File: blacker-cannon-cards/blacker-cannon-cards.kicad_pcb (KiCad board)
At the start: 2 copper layers, 85 x 55 mm, 2 parts

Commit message: Add soldermask footprint for beta
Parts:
- added G***: LOGO, npfa-gdbg:F_beta_mask_403dpi, F.Cu at (92.5, 77.5)
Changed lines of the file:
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@@
     (tracks 0)
     (zones 0)
-    (modules 2)
+    (modules 3)
     (nets 1)
   )
@@
     (uvia_drill 0.1)
   )
+  (module npfa-gdbg:F_beta_mask_403dpi (layer F.Cu)
+    (at 92.5 77.5)
+    (fp_text reference G*** (at 0 0) (layer F.SilkS) hide
+      (effects (font (size 1.524 1.524) (thickness 0.3)))
+    )
+    (fp_text value LOGO (at 0.75 0) (layer F.SilkS) hide
+      (effects (font (size 1.524 1.524) (thickness 0.3)))
+    )
+    (fp_poly (pts (xy 32.227408 -4.819358) (xy 32.535706 -4.69041) (xy 32.784801 -4.451038) (xy 32.827088 -4.390906)
+      (xy 32.899712 -4.272928) (xy 32.947698 -4.161016) (xy 32.976113 -4.025469) (xy 32.990026 -3.83659)
+      (xy 32.994502 -3.564677) (xy 32.994789 -3.408077) (xy 32.991513 -3.074074) (xy 32.978466 -2.832117)
+      (xy 32.950821 -2.648296) (xy 32.90375 -2.488699) (xy 32.843158 -2.342984) (xy 32.749223 -2.152467)
+      (xy 32.675218 -2.0578) (xy 32.599291 -2.035903) (xy 32.559535 -2.043405) (xy 32.420993 -2.071941)
+      (xy 32.216129 -2.104159) (xy 32.098499 -2.119676) (xy 31.837109 -2.120552) (xy 31.631524 -2.064004)
+      (xy 31.496214 -1.965455) (xy 31.445648 -1.840329) (xy 31.494295 -1.704052) (xy 31.610749 -1.599722)
+      (xy 31.732101 -1.542244) (xy 31.889873 -1.518741) (xy 32.122254 -1.52485) (xy 32.208043 -1.531452)
+      (xy 32.645209 -1.568103) (xy 32.833902 -1.339186) (xy 33.055745 -0.993254) (xy 33.234848 -0.563141)
+      (xy 33.362199 -0.086127) (xy 33.428786 0.400511) (xy 33.425598 0.859494) (xy 33.404099 1.019568)
+      (xy 33.344162 1.283237) (xy 33.264307 1.541713) (xy 33.207124 1.68321) (xy 32.981107 2.02351)
+      (xy 32.682619 2.269057) (xy 32.330279 2.412232) (xy 31.942707 2.445414) (xy 31.545161 2.36335)
+      (xy 31.35259 2.262869) (xy 31.146453 2.107654) (xy 31.053742 2.018737) (xy 30.814433 1.763306)
+      (xy 30.833147 -1.119464) (xy 30.83786 -1.801376) (xy 30.842697 -2.368898) (xy 30.848172 -2.833693)
+      (xy 30.854801 -3.207424) (xy 30.863098 -3.501756) (xy 30.873579 -3.728353) (xy 30.886758 -3.898877)
+      (xy 30.903151 -4.024992) (xy 30.923272 -4.118362) (xy 30.947637 -4.19065) (xy 30.971028 -4.242143)
+      (xy 31.184483 -4.54193) (xy 31.473638 -4.742293) (xy 31.829453 -4.83713) (xy 31.856148 -4.83962)
+      (xy 32.227408 -4.819358)) (layer F.Mask) (width 0.01))
+    (fp_poly (pts (xy 40.746813 0) (xy 36.272208 4.474938) (xy 35.6484 5.098482) (xy 35.049783 5.69624)
+      (xy 34.482362 6.262251) (xy 33.952141 6.790551) (xy 33.465122 7.27518) (xy 33.027311 7.710176)
+      (xy 32.64471 8.089576) (xy 32.323324 8.407419) (xy 32.069157 8.657743) (xy 31.888213 8.834585)
+      (xy 31.786495 8.931985) (xy 31.765756 8.949876) (xy 31.717706 8.906267) (xy 31.58661 8.779423)
+      (xy 31.378483 8.575315) (xy 31.09934 8.299916) (xy 30.755195 7.959198) (xy 30.352063 7.559134)
+      (xy 29.895959 7.105696) (xy 29.392896 6.604856) (xy 28.84889 6.062586) (xy 28.269955 5.48486)
+      (xy 27.88172 5.097033) (xy 29.642731 5.097033) (xy 29.66886 5.139189) (xy 29.755053 5.160222)
+      (xy 29.925413 5.167458) (xy 30.119111 5.168238) (xy 30.617796 5.168238) (xy 30.69066 4.774318)
+      (xy 30.718994 4.569504) (xy 30.747625 4.272722) (xy 30.773837 3.918024) (xy 30.794912 3.539461)
+      (xy 30.801397 3.386312) (xy 30.83927 2.392227) (xy 30.97162 2.490259) (xy 31.362689 2.704946)
+      (xy 31.813252 2.825269) (xy 32.296132 2.848393) (xy 32.78415 2.771483) (xy 33.002093 2.702028)
+      (xy 33.381878 2.502552) (xy 33.741414 2.208051) (xy 34.048127 1.848953) (xy 34.219087 1.565245)
+      (xy 34.427678 1.027591) (xy 34.522226 0.491316) (xy 34.505964 -0.029643) (xy 34.382125 -0.521345)
+      (xy 34.153945 -0.969852) (xy 33.824657 -1.361225) (xy 33.477194 -1.632485) (xy 33.175241 -1.826248)
+      (xy 33.500605 -2.162168) (xy 33.775751 -2.504121) (xy 33.946129 -2.866736) (xy 34.024589 -3.282887)
+      (xy 34.033355 -3.524999) (xy 33.975794 -3.989551) (xy 33.81183 -4.394554) (xy 33.549609 -4.733072)
+      (xy 33.197276 -4.998174) (xy 32.762975 -5.182925) (xy 32.254853 -5.280393) (xy 31.954838 -5.294293)
+      (xy 31.43413 -5.247205) (xy 30.980339 -5.101818) (xy 30.574328 -4.851945) (xy 30.56584 -4.845267)
+      (xy 30.27622 -4.555881) (xy 30.066757 -4.201489) (xy 29.928278 -3.763656) (xy 29.876248 -3.459449)
+      (xy 29.864843 -3.308956) (xy 29.854053 -3.045755) (xy 29.844088 -2.683193) (xy 29.835159 -2.234615)
+      (xy 29.827474 -1.713367) (xy 29.821245 -1.132796) (xy 29.816681 -0.506247) (xy 29.813992 0.152933)
+      (xy 29.81338 0.535732) (xy 29.812047 1.360555) (xy 29.809002 2.070257) (xy 29.803853 2.675765)
+      (xy 29.796211 3.188005) (xy 29.785683 3.617905) (xy 29.771878 3.976391) (xy 29.754405 4.274389)
+      (xy 29.732872 4.522827) (xy 29.706889 4.732632) (xy 29.676064 4.914729) (xy 29.652563 5.026427)
+      (xy 29.642731 5.097033) (xy 27.88172 5.097033) (xy 27.662105 4.877649) (xy 27.274895 4.490529)
+      (xy 22.81588 0.031183) (xy 27.306741 -4.459348) (xy 31.797601 -8.949878) (xy 40.746813 0)) (layer F.Mask) (width 0.01))
+  )
   (module npfa-gdbg:F_silk_403dpi (layer F.Cu)

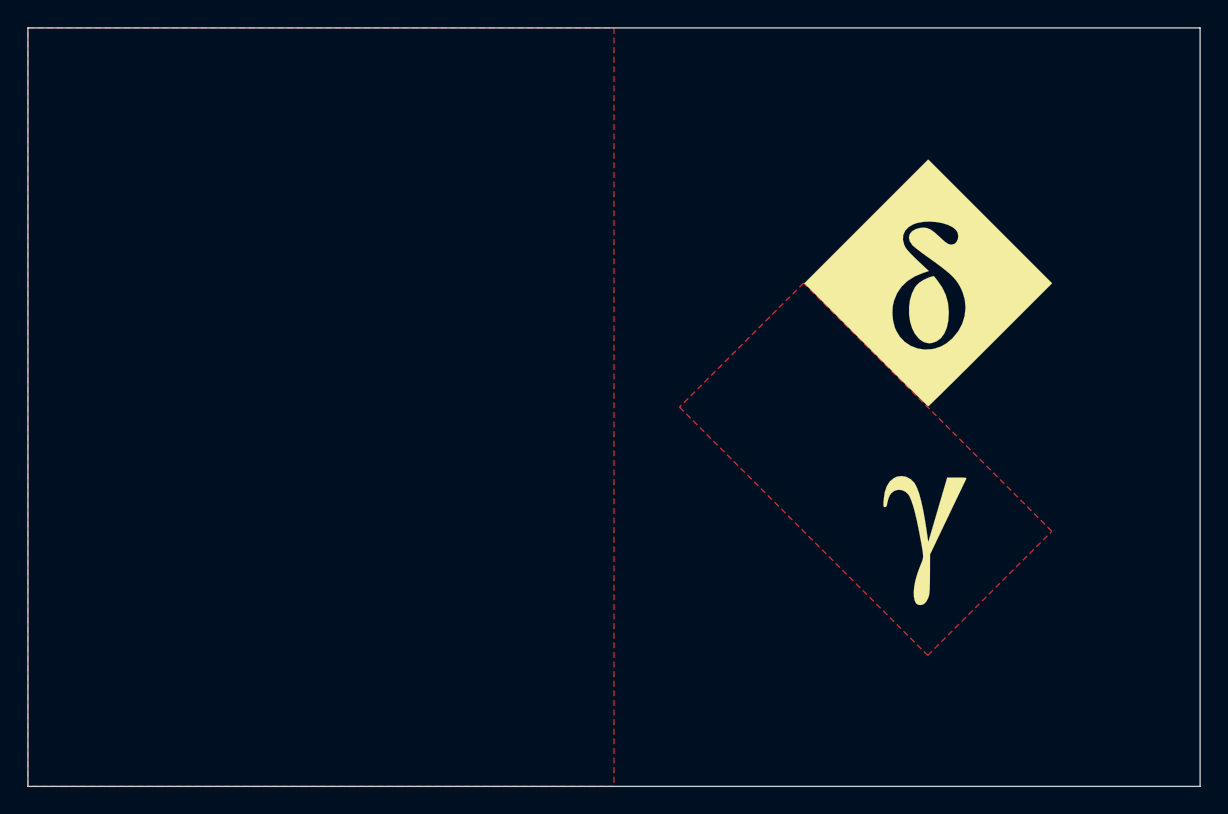
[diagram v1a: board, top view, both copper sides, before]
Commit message: Center diamond on right side
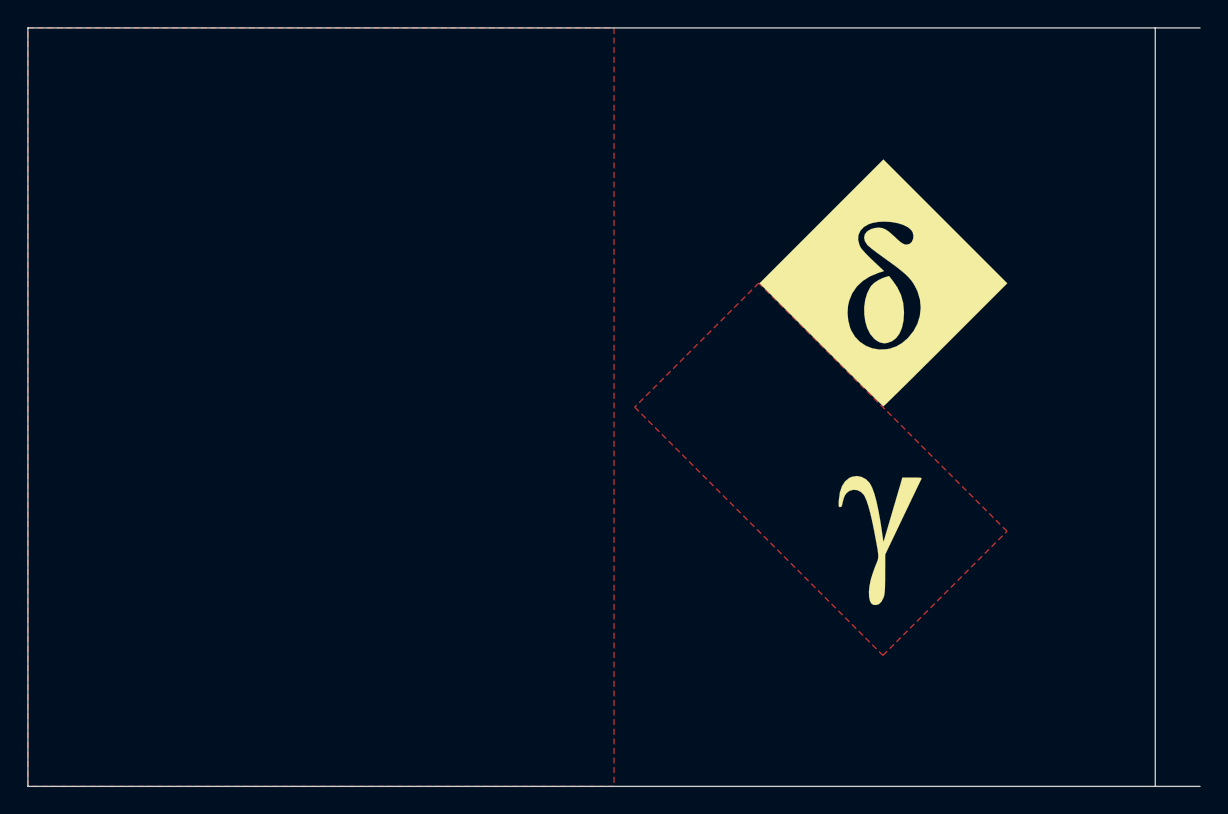
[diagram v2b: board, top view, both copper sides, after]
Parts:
- moved G*** 3.25 mm to (89.2, 77.5) (x3)
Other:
- outline, holes or cut-outs redrawn
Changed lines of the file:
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@@
     (solder_mask_min_width 0.25)
     (aux_axis_origin 0 0)
-    (visible_elements FFFFFF7F)
+    (visible_elements 7FFFFFFF)
     (pcbplotparams
       (layerselection 0x010fc_ffffffff)
@@
   )
   (module npfa-gdbg:F_beta_mask_403dpi (layer F.Cu)
-    (at 92.5 77.5)
+    (at 89.25 77.5)
     (fp_text reference G*** (at 0 0) (layer F.SilkS) hide
       (effects (font (size 1.524 1.524) (thickness 0.3)))
@@
   )
   (module npfa-gdbg:F_silk_403dpi (layer F.Cu)
-    (at 92.5 77.5)
+    (at 89.25 77.5)
     (fp_text reference G*** (at 0 0) (layer F.SilkS) hide
       (effects (font (size 1.524 1.524) (thickness 0.3)))
@@
   )
   (module npfa-gdbg:F_gamma_eng_fp_403dpi (layer F.Cu)
-    (at 92.5 77.5)
+    (at 89.25 77.5)
     (fp_text reference G*** (at 0 0) (layer F.SilkS) hide
       (effects (font (size 1.524 1.524) (thickness 0.3)))
@@
   )
   (gr_line (start 135 50) (end 50 50) (layer Edge.Cuts) (width 0.05))
-  (gr_line (start 135 105) (end 135 50) (layer Edge.Cuts) (width 0.05))
+  (gr_line (start 131.75 105) (end 131.75 50) (layer Edge.Cuts) (width 0.05))
   (gr_line (start 50 105) (end 135 105) (layer Edge.Cuts) (width 0.05))
   (gr_line (start 50 50) (end 50 105) (layer Edge.Cuts) (width 0.05))
@@
   )
   (gr_line (start 135 50) (end 50 50) (layer Dwgs.User) (width 0.15))
-  (gr_line (start 135 105) (end 135 50) (layer Dwgs.User) (width 0.15))
+  (gr_line (start 131.75 105) (end 131.75 50) (layer Dwgs.User) (width 0.15))
   (gr_line (start 50 105) (end 135 105) (layer Dwgs.User) (width 0.15))
   (gr_line (start 50 50) (end 50 105) (layer Dwgs.User) (width 0.15))
@@
     (polygon
       (pts
-        (xy 97.25 77.5) (xy 115.25 95.5) (xy 124.25 86.5) (xy 106.25 68.5)
+        (xy 94 77.5) (xy 112 95.5) (xy 121 86.5) (xy 103 68.5)
       )
     )

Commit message: Actually center it
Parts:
- moved G*** 2.00 mm to (91.2, 77.5) (x3)
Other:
- outline, holes or cut-outs redrawn
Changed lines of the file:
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@@
   )
   (module npfa-gdbg:F_beta_mask_403dpi (layer F.Cu)
-    (at 89.25 77.5)
+    (at 91.25 77.5)
     (fp_text reference G*** (at 0 0) (layer F.SilkS) hide
       (effects (font (size 1.524 1.524) (thickness 0.3)))
@@
   )
   (module npfa-gdbg:F_silk_403dpi (layer F.Cu)
-    (at 89.25 77.5)
+    (at 91.25 77.5)
     (fp_text reference G*** (at 0 0) (layer F.SilkS) hide
       (effects (font (size 1.524 1.524) (thickness 0.3)))
@@
   )
   (module npfa-gdbg:F_gamma_eng_fp_403dpi (layer F.Cu)
-    (at 89.25 77.5)
+    (at 91.25 77.5)
     (fp_text reference G*** (at 0 0) (layer F.SilkS) hide
       (effects (font (size 1.524 1.524) (thickness 0.3)))
@@
   )
   (gr_line (start 135 50) (end 50 50) (layer Edge.Cuts) (width 0.05))
-  (gr_line (start 131.75 105) (end 131.75 50) (layer Edge.Cuts) (width 0.05))
+  (gr_line (start 135 105) (end 135 50) (layer Edge.Cuts) (width 0.05))
   (gr_line (start 50 105) (end 135 105) (layer Edge.Cuts) (width 0.05))
   (gr_line (start 50 50) (end 50 105) (layer Edge.Cuts) (width 0.05))
@@
   )
   (gr_line (start 135 50) (end 50 50) (layer Dwgs.User) (width 0.15))
-  (gr_line (start 131.75 105) (end 131.75 50) (layer Dwgs.User) (width 0.15))
+  (gr_line (start 135 105) (end 135 50) (layer Dwgs.User) (width 0.15))
   (gr_line (start 50 105) (end 135 105) (layer Dwgs.User) (width 0.15))
   (gr_line (start 50 50) (end 50 105) (layer Dwgs.User) (width 0.15))
@@
     (polygon
       (pts
-        (xy 94 77.5) (xy 112 95.5) (xy 121 86.5) (xy 103 68.5)
+        (xy 95.99729 77.50271) (xy 113.99729 95.50271) (xy 122.99729 86.50271) (xy 104.99729 68.50271)
       )
     )

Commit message: Add mushroom back
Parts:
- added G***: LOGO, mushroom:B_bareboard_mask_566dpi, F.Cu at (92.5, 77.5)
- added G***: LOGO, mushroom:B_cu_566dpi, F.Cu at (92.5, 77.5)
- added G***: LOGO, mushroom:B_mask_566dpi, F.Cu at (92.5, 77.5)
- added G***: LOGO, mushroom:B_silk_566dpi, F.Cu at (92.5, 77.5)
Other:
- outline, holes or cut-outs redrawn
